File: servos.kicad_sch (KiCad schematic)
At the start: 24 parts, among them U2 PCA9685PW, U7 PCA9685PW

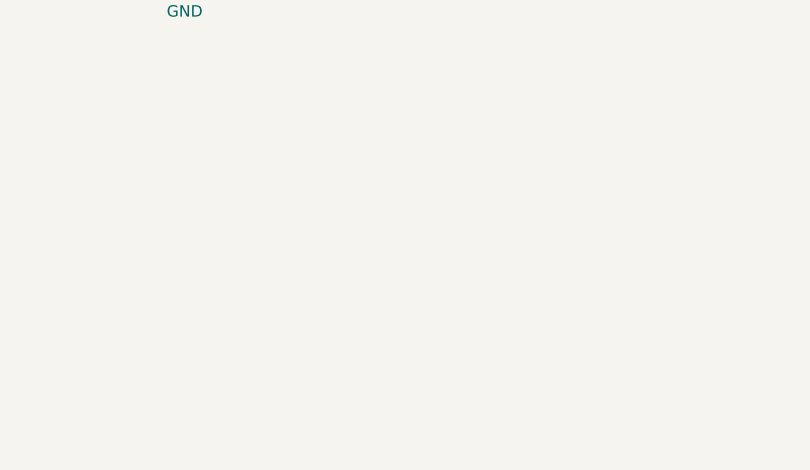
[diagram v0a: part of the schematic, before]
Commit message: Very minor tweaks for board version 3.
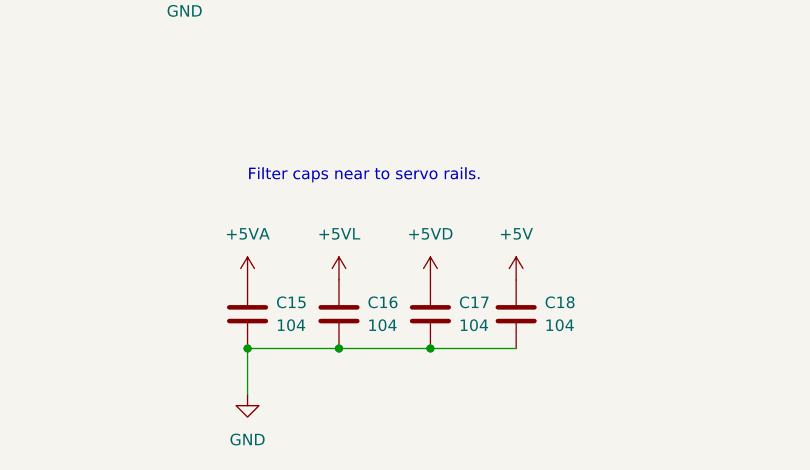
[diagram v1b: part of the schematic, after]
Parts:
- added C15, C16, C17, C18: 104, Capacitor_SMD:C_1206_3216Metric_Pad1.33x1.80mm_HandSolder, symbol Device:C
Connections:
- net +5V: now also C18.1
- net +5VA: now also C15.1
- net +5VD: now also C17.1
- net +5VL: now also C16.1
- net GND: now also C15.2, C16.2, C17.2, C18.2
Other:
- note added: "Filter caps near to servo rails."
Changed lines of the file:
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@@
   (junction (at 33.02 91.44) (diameter 0) (color 0 0 0 0)
   )
+  (junction (at 60.325 257.175) (diameter 0) (color 0 0 0 0)
+  )
   (junction (at 133.35 152.4) (diameter 0) (color 0 0 0 0)
   )
@@
   (junction (at 33.02 81.28) (diameter 0) (color 0 0 0 0)
   )
+  (junction (at 40.005 257.175) (diameter 0) (color 0 0 0 0)
+  )
   (junction (at 43.18 44.45) (diameter 0) (color 0 0 0 0)
   )
@@
   (junction (at 133.35 162.56) (diameter 0) (color 0 0 0 0)
   )
+  (junction (at 50.165 257.175) (diameter 0) (color 0 0 0 0)
+  )
   (junction (at 133.35 195.58) (diameter 0) (color 0 0 0 0)
   )
@@
     (stroke (width 0) (type default) (color 0 0 0 0))
   )
+  (wire (pts (xy 60.325 257.175) (xy 50.165 257.175))
+    (stroke (width 0) (type default) (color 0 0 0 0))
+  )
   (wire (pts (xy 29.21 180.34) (xy 29.21 179.07))
     (stroke (width 0) (type default) (color 0 0 0 0))
@@
     (stroke (width 0) (type default) (color 0 0 0 0))
   )
+  (wire (pts (xy 50.165 257.175) (xy 40.005 257.175))
+    (stroke (width 0) (type default) (color 0 0 0 0))
+  )
   (wire (pts (xy 115.57 53.34) (xy 133.35 53.34))
     (stroke (width 0) (type default) (color 0 0 0 0))
@@
     (stroke (width 0) (type default) (color 0 0 0 0))
   )
+  (wire (pts (xy 69.85 257.175) (xy 60.325 257.175))
+    (stroke (width 0) (type default) (color 0 0 0 0))
+  )
   (wire (pts (xy 143.51 46.99) (xy 152.4 46.99))
     (stroke (width 0) (type default) (color 0 0 0 0))
@@
     (stroke (width 0) (type default) (color 0 0 0 0))
   )
+  (wire (pts (xy 40.005 257.175) (xy 40.005 262.255))
+    (stroke (width 0) (type default) (color 0 0 0 0))
+  )
   (wire (pts (xy 82.55 97.79) (xy 91.44 97.79))
     (stroke (width 0) (type default) (color 0 0 0 0))
@@
   (wire (pts (xy 33.02 91.44) (xy 33.02 88.9))
     (stroke (width 0) (type default) (color 0 0 0 0))
+  )
+  (text "Filter caps near to servo rails." (at 40.005 238.76 0)
+    (effects (font (size 1.27 1.27)) (justify left bottom))
   )
   (label "PWM23" (at 143.51 153.67 0)
@@
     )
     (property "Datasheet" "" (id 3) (at 127 55.88 0)
+      (effects (font (size 1.27 1.27)) hide)
+    )
+    (pin "1")
+  )
+  (symbol (lib_id "power:GND") (at 40.005 262.255 0) (unit 1)
+    (in_bom yes) (on_board yes) (fields_autoplaced)
+    (property "Reference" "#PWR0194" (id 0) (at 40.005 268.605 0)
+      (effects (font (size 1.27 1.27)) hide)
+    )
+    (property "Value" "GND" (id 1) (at 40.005 267.335 0))
+    (property "Footprint" "" (id 2) (at 40.005 262.255 0)
+      (effects (font (size 1.27 1.27)) hide)
+    )
+    (property "Datasheet" "" (id 3) (at 40.005 262.255 0)
       (effects (font (size 1.27 1.27)) hide)
     )
@@
     (pin "1")
   )
+  (symbol (lib_id "power:+5VA") (at 40.005 249.555 0) (unit 1)
+    (in_bom yes) (on_board yes) (fields_autoplaced)
+    (property "Reference" "#PWR0193" (id 0) (at 40.005 253.365 0)
+      (effects (font (size 1.27 1.27)) hide)
+    )
+    (property "Value" "+5VA" (id 1) (at 40.005 244.475 0))
+    (property "Footprint" "" (id 2) (at 40.005 249.555 0)
+      (effects (font (size 1.27 1.27)) hide)
+    )
+    (property "Datasheet" "" (id 3) (at 40.005 249.555 0)
+      (effects (font (size 1.27 1.27)) hide)
+    )
+    (pin "1")
+  )
   (symbol (lib_id "power:+5V") (at 194.31 63.5 0) (unit 1)
     (in_bom yes) (on_board yes) (fields_autoplaced)
@@
     (pin "1")
   )
+  (symbol (lib_id "Device:C") (at 50.165 253.365 0) (unit 1)
+    (in_bom yes) (on_board yes) (fields_autoplaced)
+    (property "Reference" "C16" (id 0) (at 53.34 252.0949 0)
+      (effects (font (size 1.27 1.27)) (justify left))
+    )
+    (property "Value" "104" (id 1) (at 53.34 254.6349 0)
+      (effects (font (size 1.27 1.27)) (justify left))
+    )
+    (property "Footprint" "Capacitor_SMD:C_1206_3216Metric_Pad1.33x1.80mm_HandSolder" (id 2) (at 51.1302 257.175 0)
+      (effects (font (size 1.27 1.27)) hide)
+    )
+    (property "Datasheet" "~" (id 3) (at 50.165 253.365 0)
+      (effects (font (size 1.27 1.27)) hide)
+    )
+    (pin "1")
+    (pin "2")
+  )
+  (symbol (lib_id "Device:C") (at 69.85 253.365 0) (unit 1)
+    (in_bom yes) (on_board yes) (fields_autoplaced)
+    (property "Reference" "C18" (id 0) (at 73.025 252.0949 0)
+      (effects (font (size 1.27 1.27)) (justify left))
+    )
+    (property "Value" "104" (id 1) (at 73.025 254.6349 0)
+      (effects (font (size 1.27 1.27)) (justify left))
+    )
+    (property "Footprint" "Capacitor_SMD:C_1206_3216Metric_Pad1.33x1.80mm_HandSolder" (id 2) (at 70.8152 257.175 0)
+      (effects (font (size 1.27 1.27)) hide)
+    )
+    (property "Datasheet" "~" (id 3) (at 69.85 253.365 0)
+      (effects (font (size 1.27 1.27)) hide)
+    )
+    (pin "1")
+    (pin "2")
+  )
   (symbol (lib_id "power:GND") (at 187.96 218.44 0) (unit 1)
     (in_bom yes) (on_board yes) (fields_autoplaced)
@@
     (pin "1")
   )
+  (symbol (lib_id "Device:C") (at 40.005 253.365 0) (unit 1)
+    (in_bom yes) (on_board yes) (fields_autoplaced)
+    (property "Reference" "C15" (id 0) (at 43.18 252.0949 0)
+      (effects (font (size 1.27 1.27)) (justify left))
+    )
+    (property "Value" "104" (id 1) (at 43.18 254.6349 0)
+      (effects (font (size 1.27 1.27)) (justify left))
+    )
+    (property "Footprint" "Capacitor_SMD:C_1206_3216Metric_Pad1.33x1.80mm_HandSolder" (id 2) (at 40.9702 257.175 0)
+      (effects (font (size 1.27 1.27)) hide)
+    )
+    (property "Datasheet" "~" (id 3) (at 40.005 253.365 0)
+      (effects (font (size 1.27 1.27)) hide)
+    )
+    (pin "1")
+    (pin "2")
+  )
   (symbol (lib_id "Adafruit:HEADER-3X04") (at 115.57 48.26 0) (unit 1)
     (in_bom yes) (on_board yes) (fields_autoplaced)
@@
     )
     (pin "1")
+  )
+  (symbol (lib_id "Device:C") (at 60.325 253.365 0) (unit 1)
+    (in_bom yes) (on_board yes) (fields_autoplaced)
+    (property "Reference" "C17" (id 0) (at 63.5 252.0949 0)
+      (effects (font (size 1.27 1.27)) (justify left))
+    )
+    (property "Value" "104" (id 1) (at 63.5 254.6349 0)
+      (effects (font (size 1.27 1.27)) (justify left))
+    )
+    (property "Footprint" "Capacitor_SMD:C_1206_3216Metric_Pad1.33x1.80mm_HandSolder" (id 2) (at 61.2902 257.175 0)
+      (effects (font (size 1.27 1.27)) hide)
+    )
+    (property "Datasheet" "~" (id 3) (at 60.325 253.365 0)
+      (effects (font (size 1.27 1.27)) hide)
+    )
+    (pin "1")
+    (pin "2")
   )
   (symbol (lib_id "Driver_LED:PCA9685PW") (at 50.8 73.66 0) (unit 1)
@@
     (pin "1")
   )
+  (symbol (lib_id "power:+5VD") (at 60.325 249.555 0) (unit 1)
+    (in_bom yes) (on_board yes) (fields_autoplaced)
+    (property "Reference" "#PWR0187" (id 0) (at 60.325 253.365 0)
+      (effects (font (size 1.27 1.27)) hide)
+    )
+    (property "Value" "+5VD" (id 1) (at 60.325 244.475 0))
+    (property "Footprint" "" (id 2) (at 60.325 249.555 0)
+      (effects (font (size 1.27 1.27)) hide)
+    )
+    (property "Datasheet" "" (id 3) (at 60.325 249.555 0)
+      (effects (font (size 1.27 1.27)) hide)
+    )
+    (pin "1")
+  )
   (symbol (lib_id "Device:R_Pack04") (at 157.48 209.55 90) (unit 1)
     (in_bom yes) (on_board yes) (fields_autoplaced)
@@
     )
     (property "Datasheet" "" (id 3) (at 22.86 172.72 0)
+      (effects (font (size 1.27 1.27)) hide)
+    )
+    (pin "1")
+  )
+  (symbol (lib_id "power:+5V") (at 69.85 249.555 0) (unit 1)
+    (in_bom yes) (on_board yes) (fields_autoplaced)
+    (property "Reference" "#PWR0188" (id 0) (at 69.85 253.365 0)
+      (effects (font (size 1.27 1.27)) hide)
+    )
+    (property "Value" "+5V" (id 1) (at 69.85 244.475 0))
+    (property "Footprint" "" (id 2) (at 69.85 249.555 0)
+      (effects (font (size 1.27 1.27)) hide)
+    )
+    (property "Datasheet" "" (id 3) (at 69.85 249.555 0)
       (effects (font (size 1.27 1.27)) hide)
     )
@@
     (pin "9")
   )
+  (symbol (lib_id "power:+5VL") (at 50.165 249.555 0) (unit 1)
+    (in_bom yes) (on_board yes)
+    (property "Reference" "#PWR0191" (id 0) (at 50.165 253.365 0)
+      (effects (font (size 1.27 1.27)) hide)
+    )
+    (property "Value" "+5VL" (id 1) (at 50.165 244.475 0))
+    (property "Footprint" "" (id 2) (at 50.165 249.555 0)
+      (effects (font (size 1.27 1.27)) hide)
+    )
+    (property "Datasheet" "" (id 3) (at 50.165 249.555 0)
+      (effects (font (size 1.27 1.27)) hide)
+    )
+    (pin "1")
+  )
   (symbol (lib_id "Device:R_Pack04") (at 157.48 100.33 90) (unit 1)

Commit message: Finished routing board revision 3: ready for first PCB run.
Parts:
- added TP3: SCL_1, TestPoint:TestPoint_Pad_D2.0mm, symbol Connector:TestPoint
- added TP3: SDA_1, TestPoint:TestPoint_Pad_D2.0mm, symbol Connector:TestPoint
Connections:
- net WIRE_1_SCL: now also TP3.1
- net WIRE_1_SDA: now also TP3.1
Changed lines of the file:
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@@
+    (stroke (width 0) (type default))
+  )
+  (wire (pts (xy 74.295 24.13) (xy 79.375 24.13))
     (stroke (width 0) (type default))
   )
@@
     (stroke (width 0) (type default))
   )
+  (wire (pts (xy 74.295 28.575) (xy 79.375 28.575))
+    (stroke (width 0) (type default))
+  )
   (wire (pts (xy 168.91 209.55) (xy 168.91 203.2))
     (stroke (width 0) (type default))
@@
   (label "PWM2" (at 83.82 46.99 0) (fields_autoplaced)
     (effects (font (size 1.27 1.27)) (justify left bottom))
+  )
+  (global_label "WIRE_1_SCL" (shape input) (at 74.295 24.13 180) (fields_autoplaced)
+    (effects (font (size 1.27 1.27)) (justify right))
+    (property "Intersheetrefs" "${INTERSHEET_REFS}" (at 60.7543 24.0506 0)
+      (effects (font (size 1.27 1.27)) (justify right) hide)
+    )
   )
   (global_label "WIRE_1_SDA" (shape input) (at 29.21 166.37 180) (fields_autoplaced)
@@
     (effects (font (size 1.27 1.27)) (justify right))
     (property "Intersheetrefs" "${INTERSHEET_REFS}" (at 15.6693 163.7506 0)
+      (effects (font (size 1.27 1.27)) (justify right) hide)
+    )
+  )
+  (global_label "WIRE_1_SDA" (shape input) (at 74.295 28.575 180) (fields_autoplaced)
+    (effects (font (size 1.27 1.27)) (justify right))
+    (property "Intersheetrefs" "${INTERSHEET_REFS}" (at 60.6938 28.4956 0)
       (effects (font (size 1.27 1.27)) (justify right) hide)
     )
@@
     )
   )
+  (symbol (lib_id "Connector:TestPoint") (at 79.375 24.13 270) (mirror x) (unit 1)
+    (in_bom yes) (on_board yes) (dnp no)
+    (property "Reference" "TP3" (at 85.725 24.13 90)
+      (effects (font (size 1.27 1.27)))
+    )
+    (property "Value" "SCL_1" (at 82.677 21.59 90)
+      (effects (font (size 1.27 1.27)))
+    )
+    (property "Footprint" "TestPoint:TestPoint_Pad_D2.0mm" (at 79.375 19.05 0)
+      (effects (font (size 1.27 1.27)) hide)
+    )
+    (property "Datasheet" "~" (at 79.375 19.05 0)
+      (effects (font (size 1.27 1.27)) hide)
+    )
+    (pin "1")
+    (instances
+      (project "robot"
+        (path "/762e1435-54f1-40a1-a522-bcedd8174116/78a56bae-3afa-4383-914f-3e74817e0e83"
+          (reference "TP3") (unit 1)
+        )
+        (path "/762e1435-54f1-40a1-a522-bcedd8174116/69ddaad4-6a4d-496c-81a2-3d2ec8ddf76d"
+          (reference "TP5") (unit 1)
+        )
+      )
+    )
+  )
   (symbol (lib_id "power:+5VD") (at 133.35 116.84 0) (unit 1)
     (in_bom yes) (on_board yes) (dnp no) (fields_autoplaced)
@@
         )
       )
+    )
+  )
+  (symbol (lib_id "Connector:TestPoint") (at 79.375 28.575 270) (mirror x) (unit 1)
+    (in_bom yes) (on_board yes) (dnp no)
+    (property "Reference" "TP3" (at 85.725 28.575 90)
+      (effects (font (size 1.27 1.27)))
+    )
+    (property "Value" "SDA_1" (at 83.185 31.115 90)
+      (effects (font (size 1.27 1.27)))
+    )
+    (property "Footprint" "TestPoint:TestPoint_Pad_D2.0mm" (at 79.375 23.495 0)
+      (effects (font (size 1.27 1.27)) hide)
+    )
+    (property "Datasheet" "~" (at 79.375 23.495 0)
+      (effects (font (size 1.27 1.27)) hide)
+    )
+    (pin "1")
+    (instances
+      (project "robot"
+        (path "/762e1435-54f1-40a1-a522-bcedd8174116/78a56bae-3afa-4383-914f-3e74817e0e83"
+          (reference "TP3") (unit 1)
+        )
+        (path "/762e1435-54f1-40a1-a522-bcedd8174116/69ddaad4-6a4d-496c-81a2-3d2ec8ddf76d"
+          (reference "TP6") (unit 1)
+        )
+      )
